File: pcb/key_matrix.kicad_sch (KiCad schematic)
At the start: 138 parts, among them K1 KEYSW, K10 KEYSW, K11 KEYSW, K12 KEYSW, K13 KEYSW, K14 KEYSW, K15 KEYSW, K16 KEYSW, K17 KEYSW, K18 KEYSW, K19 KEYSW, K2 KEYSW, K20 KEYSW, K21 KEYSW, K22 KEYSW, K23 KEYSW, K24 KEYSW, K25 KEYSW, K26 KEYSW, K27 KEYSW, K28 KEYSW, K29 KEYSW, K3 KEYSW, K30 KEYSW, K31 KEYSW, K32 KEYSW, K33 KEYSW, K34 KEYSW, K35 KEYSW, K36 KEYSW, K37 KEYSW, K38 KEYSW, K39 KEYSW, K4 KEYSW, K40 KEYSW, K41 KEYSW, K42 KEYSW, K43 KEYSW, K45 KEYSW, K46 KEYSW, K47 KEYSW, K48 KEYSW, K49 KEYSW, K5 KEYSW, K50 KEYSW, K51 KEYSW, K52 KEYSW, K53 KEYSW, K54 KEYSW, K55 KEYSW, K56 KEYSW, K57 KEYSW, K58 KEYSW, K59 KEYSW, K6 KEYSW, K60 KEYSW, K61 KEYSW, K62 KEYSW, K63 KEYSW, K67 KEYSW, K7 KEYSW, K70 KEYSW, K71 KEYSW, K72 KEYSW, K73 KEYSW, K74 KEYSW, K75 KEYSW, K8 KEYSW, K9 KEYSW

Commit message: Start assigning footprints
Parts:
- D1, D10, D11, D12, D13, D14, D15, D16, D17, D18, D19, D2, D20, D21, D22, D23, D24, D25, D26, D27, D28, D29, D3, D30, D31, D32, D33, D34, D35, D36, D37, D38, D39, D4, D40, D41, D42, D43, D45, D46, D47, D48, D49, D5, D50, D51, D52, D53, D54, D55, D56, D57, D58, D59, D6, D60, D61, D62, D63, D67, D7, D70, D71, D72, D73, D74, D75, D8, D9: footprint (none) -> Diode_SMD:D_0805_2012Metric_Pad1.15x1.40mm_HandSolder
- K1, K10, K11, K12, K13, K14, K2, K3, K4, K5, K6, K7, K8, K9: footprint (none) -> Switch_Keyboard_Hotswap_Kailh:SW_Hotswap_Kailh_Choc_V1V2_1.00u
- K15: footprint (none) -> Switch_Keyboard_Hotswap_Kailh:SW_Hotswap_Kailh_Choc_V1V2_2.00u
- K30: footprint (none) -> Switch_Keyboard_Hotswap_Kailh:SW_Hotswap_Kailh_Choc_V1V2_ISOEnter

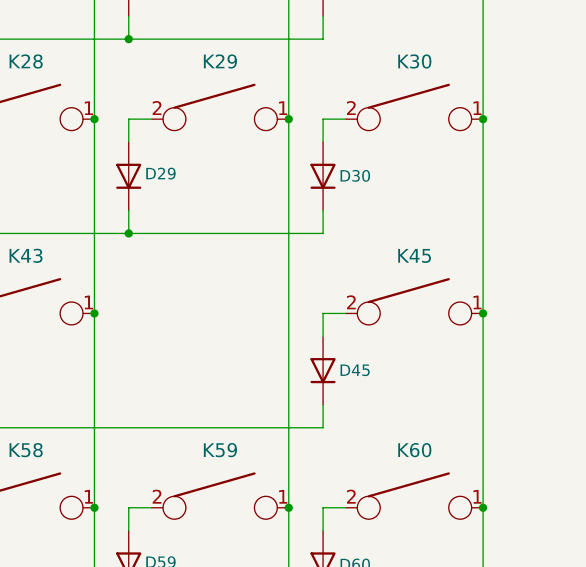
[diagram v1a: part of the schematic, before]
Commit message: Fix and complete keyswitch assignments
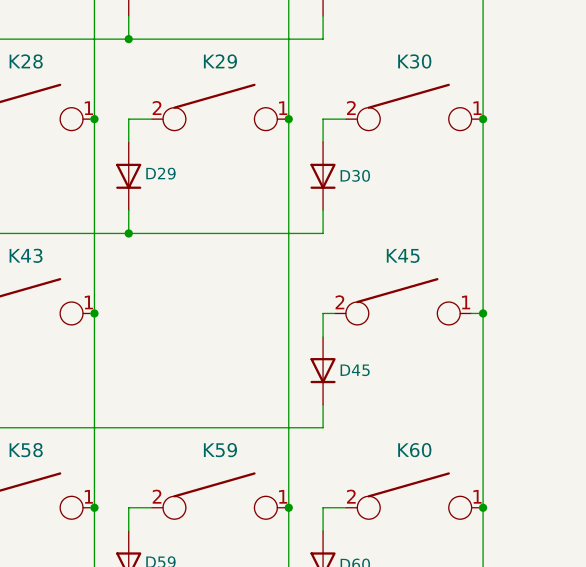
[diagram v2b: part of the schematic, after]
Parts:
- K1, K10, K11, K12, K13, K2, K3, K4, K5, K6, K7, K8, K9: footprint Switch_Keyboard_Hotswap_Kailh:SW_Hotswap_Kailh_Choc_V1V2_1.00u -> Switch_Keyboard_Hotswap_Kailh:SW_Hotswap_Kailh_MX_1.00u
- K14: footprint Switch_Keyboard_Hotswap_Kailh:SW_Hotswap_Kailh_Choc_V1V2_1.00u -> Switch_Keyboard_Hotswap_Kailh:SW_Hotswap_Kailh_MX_2.00u
- K15: footprint Switch_Keyboard_Hotswap_Kailh:SW_Hotswap_Kailh_Choc_V1V2_2.00u -> Switch_Keyboard_Hotswap_Kailh:SW_Hotswap_Kailh_MX_1.00u
- K16: footprint (none) -> Switch_Keyboard_Hotswap_Kailh:SW_Hotswap_Kailh_MX_1.50u
- K17, K18, K19, K20, K21, K22, K23, K24, K25, K26, K27, K28, K32, K33, K34, K35, K36, K37, K38, K39, K40, K41, K42, K43, K45, K47, K48, K49, K50, K51, K52, K53, K54, K55, K56, K57, K59, K60, K70, K71, K72, K73, K74, K75: footprint (none) -> Switch_Keyboard_Hotswap_Kailh:SW_Hotswap_Kailh_MX_1.00u
- K29: footprint (none) -> Switch_Keyboard_Hotswap_Kailh:SW_Hotswap_Kailh_MX_ISOEnter
- K30: footprint Switch_Keyboard_Hotswap_Kailh:SW_Hotswap_Kailh_Choc_V1V2_ISOEnter -> Switch_Keyboard_Hotswap_Kailh:SW_Hotswap_Kailh_MX_1.00u
- K31, K58: footprint (none) -> Switch_Keyboard_Hotswap_Kailh:SW_Hotswap_Kailh_MX_1.75u
- K46, K61, K62, K63: footprint (none) -> Switch_Keyboard_Hotswap_Kailh:SW_Hotswap_Kailh_MX_1.25u
- K67: footprint (none) -> Switch_Keyboard_Hotswap_Kailh:SW_Hotswap_Kailh_MX_6.25u
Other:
- moved on the sheet: K45

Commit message: Add a stabilised footprint for a 6.25u key
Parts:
- K67: footprint Switch_Keyboard_Hotswap_Kailh:SW_Hotswap_Kailh_MX_6.25u -> My_Footprints:SW_Hotswap_Kailh_MX_6.25u_Stabilised
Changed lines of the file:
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@@
 			)
 		)
-		(property "Footprint" "Switch_Keyboard_Hotswap_Kailh:SW_Hotswap_Kailh_MX_6.25u"
+		(property "Footprint" "My_Footprints:SW_Hotswap_Kailh_MX_6.25u_Stabilised"
 			(at 191.77 173.99 0)
 			(hide yes)

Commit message: Add remaining stabilised keys
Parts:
- K14: footprint Switch_Keyboard_Hotswap_Kailh:SW_Hotswap_Kailh_MX_2.00u -> My_Footprints:SW_Hotswap_Kailh_MX_2.00u_Stabilised
- K29: footprint Switch_Keyboard_Hotswap_Kailh:SW_Hotswap_Kailh_MX_ISOEnter -> My_Footprints:SW_Hotswap_Kailh_MX_ISOEnter_Stabilised
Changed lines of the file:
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@@
 			)
 		)
-		(property "Footprint" "Switch_Keyboard_Hotswap_Kailh:SW_Hotswap_Kailh_MX_2.00u"
+		(property "Footprint" "My_Footprints:SW_Hotswap_Kailh_MX_2.00u_Stabilised"
 			(at 342.9 87.63 0)
 			(hide yes)
@@
 			)
 		)
-		(property "Footprint" "Switch_Keyboard_Hotswap_Kailh:SW_Hotswap_Kailh_MX_ISOEnter"
+		(property "Footprint" "My_Footprints:SW_Hotswap_Kailh_MX_ISOEnter_Stabilised"
 			(at 342.9 109.22 0)
 			(hide yes)
